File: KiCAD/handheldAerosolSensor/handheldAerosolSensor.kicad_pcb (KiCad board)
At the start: 2 copper layers, 100 x 94.8 mm, 55 parts, among them J1 I2C 3v3, J2 ePaper, J201 PWR-OUT, J202 Ext.Sw, J3 SPS30, J4 BME/P280, J5 Ext.Sw, J6 PMS5003, Q1 AO3401, Q2 BSS138, Q201 AO3401, Q202 BC848, Q203 BC848, Q3 BSS138, SW1 PWR, SW201 PWR, U2 Mini DC-DC Convertor, U202 Mini DC-DC Convertor, U3 ESP32-DEVKIT-V1 30pin

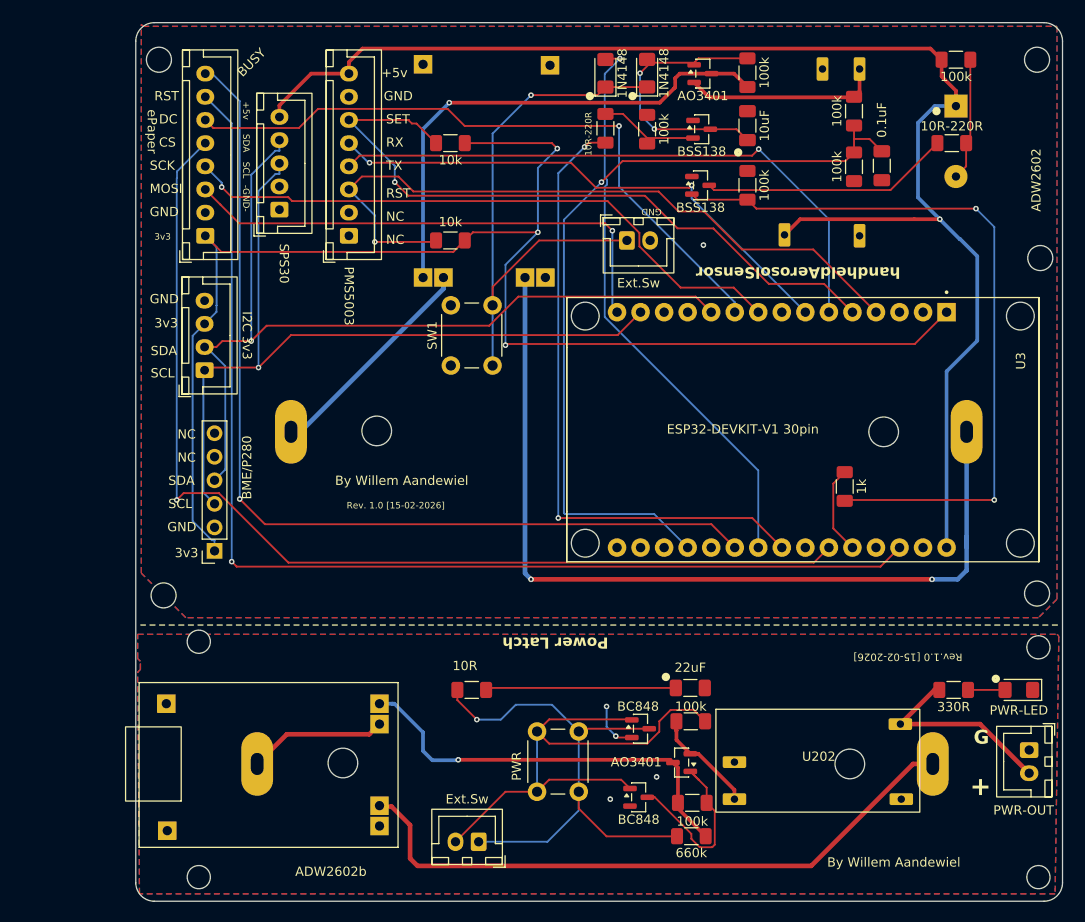
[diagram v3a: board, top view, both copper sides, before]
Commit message: Repositioned all mounting holes (H1-H5, H201-H204) to align with updated mechanical constraints. Updated board edge graphics and coordinates to match the new hole positions. Changes improve PCB fitment in enclosure.
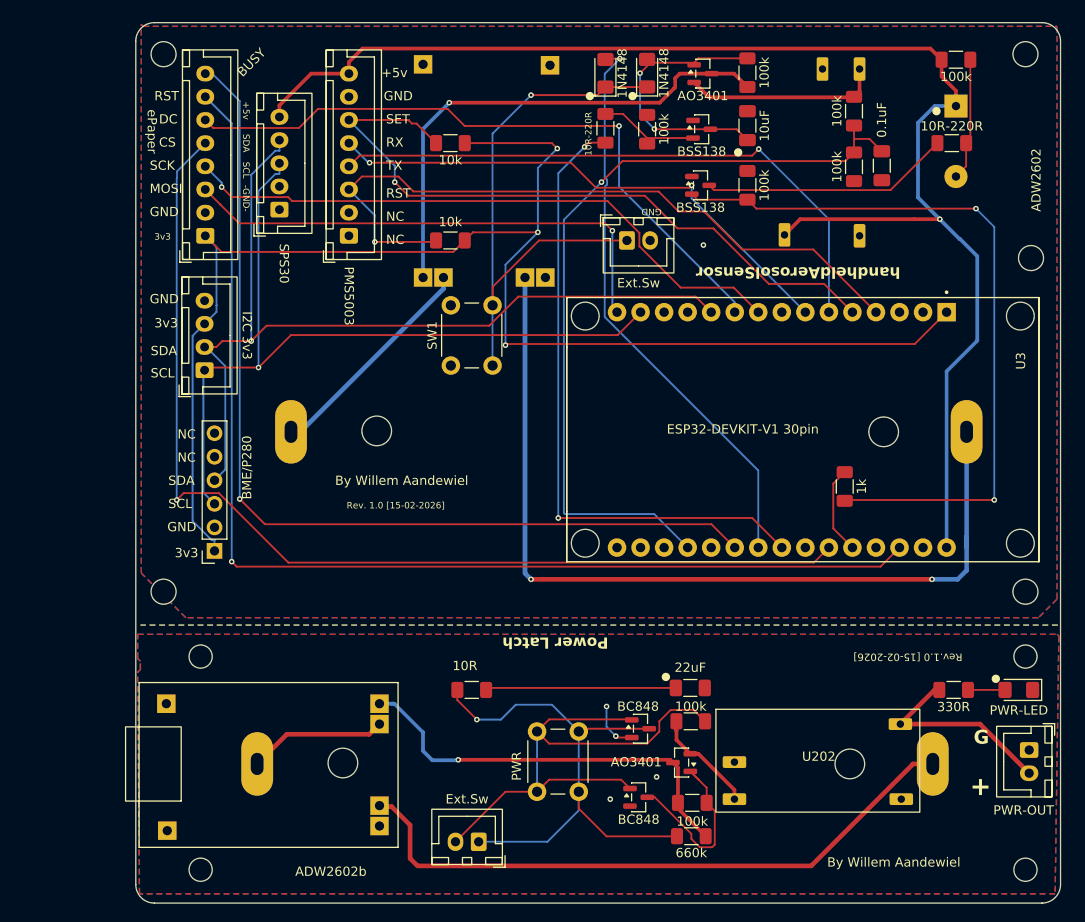
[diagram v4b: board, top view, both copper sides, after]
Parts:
- moved H202 1.72 mm to (223.0, 112.0)
- moved H203 1.61 mm to (223.0, 135.0)
- moved H201 1.61 mm to (134.0, 112.0)
- moved H2 1.39 mm to (223.0, 47.0)
- moved H3 1.27 mm to (223.0, 105.0)
- moved H5 1.00 mm to (223.6, 69.0)
- moved H204 0.82 mm to (134.0, 135.0)
- moved H1 0.78 mm to (130.0, 47.0)
- moved H4 0.40 mm to (130.0, 105.0)
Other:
- board size 100 x 94.8 mm -> 99.8 x 95 mm
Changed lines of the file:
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@@
 	(footprint "MountingHole:MountingHole_2.5mm"
 		(layer "F.Cu")
-		(at 133.8 110.4)
+		(at 134 112)
 		(descr "Mounting Hole 2.5mm, no annular, generated by kicad-footprint-generator mountinghole.py")
 		(tags "mountinghole")
@@
 	(footprint "MountingHole:MountingHole_2.7mm"
 		(layer "F.Cu")
-		(at 224.6 69)
+		(at 223.6 69)
 		(descr "Mounting Hole 2.7mm, no annular, generated by kicad-footprint-generator mountinghole.py")
 		(tags "mountinghole")
@@
 	(footprint "MountingHole:MountingHole_2.5mm"
 		(layer "F.Cu")
-		(at 224.4 111)
+		(at 223 112)
 		(descr "Mounting Hole 2.5mm, no annular, generated by kicad-footprint-generator mountinghole.py")
 		(tags "mountinghole")
@@
 	(footprint "MountingHole:MountingHole_2.5mm"
 		(layer "F.Cu")
-		(at 224.4 135.8)
+		(at 223 135)
 		(descr "Mounting Hole 2.5mm, no annular, generated by kicad-footprint-generator mountinghole.py")
 		(tags "mountinghole")
@@
 	(footprint "MountingHole:MountingHole_2.7mm"
 		(layer "F.Cu")
-		(at 130 105.4)
+		(at 130 105)
 		(descr "Mounting Hole 2.7mm, no annular, generated by kicad-footprint-generator mountinghole.py")
 		(tags "mountinghole")
@@
 	(footprint "MountingHole:MountingHole_2.7mm"
 		(layer "F.Cu")
-		(at 224.25 47.6)
+		(at 223 47)
 		(descr "Mounting Hole 2.7mm, no annular, generated by kicad-footprint-generator mountinghole.py")
 		(tags "mountinghole")
@@
 	(footprint "MountingHole:MountingHole_2.7mm"
 		(layer "F.Cu")
-		(at 224.25 105.2)
+		(at 223 105)
 		(descr "Mounting Hole 2.7mm, no annular, generated by kicad-footprint-generator mountinghole.py")
 		(tags "mountinghole")
@@
 	(footprint "MountingHole:MountingHole_2.5mm"
 		(layer "F.Cu")
-		(at 133.8 135.8)
+		(at 134 135)
 		(descr "Mounting Hole 2.5mm, no annular, generated by kicad-footprint-generator mountinghole.py")
 		(tags "mountinghole")
@@
 	(footprint "MountingHole:MountingHole_2.7mm"
 		(layer "F.Cu")
-		(at 129.5 47.6)
+		(at 130 47)
 		(descr "Mounting Hole 2.7mm, no annular, generated by kicad-footprint-generator mountinghole.py")
 		(tags "mountinghole")
@@
 	)
 	(gr_arc
-		(start 227 136.4)
-		(mid 226.414214 137.814214)
-		(end 225 138.4)
+		(start 127 45.6)
+		(mid 127.585786 44.185786)
+		(end 129 43.6)
 		(stroke
 			(width 0.05)
@@
 		(layer "Edge.Cuts")
 	)
-	(gr_arc
-		(start 129 138.4)
-		(mid 127.585786 137.814214)
-		(end 127 136.4)
+	(gr_line
+		(start 127 136.6)
+		(end 127 45.6)
 		(stroke
 			(width 0.05)
@@
 	)
 	(gr_arc
-		(start 127 45.6)
-		(mid 127.585786 44.185786)
-		(end 129 43.6)
+		(start 226.785786 136.6)
+		(mid 226.2 138.014214)
+		(end 224.785786 138.6)
 		(stroke
 			(width 0.05)
@@
 		(layer "Edge.Cuts")
 	)
-	(gr_line
-		(start 127 136.4)
-		(end 127 45.6)
+	(gr_arc
+		(start 224.785786 43.6)
+		(mid 226.2 44.185786)
+		(end 226.785786 45.6)
 		(stroke
 			(width 0.05)
@@
 	)
 	(gr_line
-		(start 225 138.4)
-		(end 129 138.4)
+		(start 129 43.6)
+		(end 224.785786 43.6)
 		(stroke
 			(width 0.05)
@@
 		(layer "Edge.Cuts")
 	)
-	(gr_line
-		(start 129 43.6)
-		(end 225 43.6)
+	(gr_arc
+		(start 129 138.6)
+		(mid 127.585786 138.014214)
+		(end 127 136.6)
 		(stroke
 			(width 0.05)
@@
 	)
 	(gr_line
-		(start 227 45.6)
-		(end 227 136.4)
+		(start 226.785786 45.6)
+		(end 226.785786 136.6)
 		(stroke
 			(width 0.05)
@@
 		(layer "Edge.Cuts")
 	)
-	(gr_arc
-		(start 225 43.6)
-		(mid 226.414214 44.185786)
-		(end 227 45.6)
+	(gr_line
+		(start 224.785786 138.6)
+		(end 129 138.6)
 		(stroke
 			(width 0.05)
@@
 		(layer "Dwgs.User")
 		(pts
-			(xy 227 45.28) (xy 127.035 45.28)
+			(xy 223.2 108.6) (xy 223.2 123.6)
 		)
-		(height -22.78)
-		(orientation 0)
+		(height 11)
+		(orientation 1)
 		(format
 			(prefix "")
@@
 			(keep_text_aligned yes)
 		)
-		(gr_text "100"
-			(at 177.0175 18.75 0)
+		(gr_text "15"
+			(at 231.8 116.1 90)
 			(layer "Dwgs.User")
 			(effects
 				(font
-					(size 3 3)
-					(thickness 3)
+					(size 2 2)
+					(thickness 0.4)
 					(bold yes)
 				)
@@
 		(layer "Dwgs.User")
 		(pts
-			(xy 223.2 108.6) (xy 223.2 123.6)
+			(xy 223.8 43.6) (xy 223.8 108.6)
 		)
-		(height 11)
+		(height 18.6)
 		(orientation 1)
 		(format
@@
 			(keep_text_aligned yes)
 		)
-		(gr_text "15"
-			(at 231.8 116.1 90)
+		(gr_text "65"
+			(at 238.8 76.1 90)
 			(layer "Dwgs.User")
 			(effects
 				(font
-					(size 2 2)
-					(thickness 0.4)
+					(size 3 3)
+					(thickness 0.6)
 					(bold yes)
 				)
@@
 		(layer "Dwgs.User")
 		(pts
-			(xy 223.8 43.6) (xy 223.8 108.6)
+			(xy 223.2 108.6) (xy 223.2 138.6)
 		)
-		(height 18.6)
+		(height 19.2)
 		(orientation 1)
 		(format
@@
 			(keep_text_aligned yes)
 		)
-		(gr_text "65"
-			(at 238.8 76.1 90)
+		(gr_text "30"
+			(at 238.8 123.6 90)
 			(layer "Dwgs.User")
 			(effects
@@
 		(layer "Dwgs.User")
 		(pts
-			(xy 223.2 108.6) (xy 223.2 138.6)
+			(xy 127 52.4) (xy 226.8 52.4)
 		)
-		(height 19.2)
-		(orientation 1)
+		(height -14.2)
+		(orientation 0)
 		(format
 			(prefix "")
@@
 			(units 3)
 			(units_format 0)
-			(precision 1)
+			(precision 4)
 			(suppress_zeroes yes)
 		)
@@
 			(keep_text_aligned yes)
 		)
-		(gr_text "30"
-			(at 238.8 123.6 90)
+		(gr_text "99.8"
+			(at 176.9 37.05 0)
 			(layer "Dwgs.User")
 			(effects
 				(font
-					(size 3 3)
-					(thickness 0.6)
-					(bold yes)
+					(size 1 1)
+					(thickness 0.15)
 				)
 			)

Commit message: KiCAD design openScad design
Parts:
- removed BT201: BH-18650-PC, MyNewLibrary:BAT_BH-18650-PC
- removed C201: 22uF, Capacitor_SMD:C_1206_3216Metric_Pad1.33x1.80mm_HandSolder
- removed D201: PWR-LED, LED_SMD:LED_1206_3216Metric_Pad1.42x1.75mm_HandSolder
- removed H201, H202, H203, H204: MountingHole, MountingHole:MountingHole_2.5mm
- removed J201: PWR-OUT, Connector_JST:JST_XH_B2B-XH-A_1x02_P2.50mm_Vertical
- removed J202: Ext.Sw, Connector_JST:JST_XH_B2B-XH-A_1x02_P2.50mm_Vertical
- removed Q1, Q201: AO3401, Package_TO_SOT_SMD:SOT-23
- removed Q2, Q3: BSS138, Package_TO_SOT_SMD:SOT-23
- removed Q202, Q203: BC848, Package_TO_SOT_SMD:SOT-23
- removed R201, R202: 100k, Resistor_SMD:R_1206_3216Metric_Pad1.30x1.75mm_HandSolder
- removed R203: 660k, Resistor_SMD:R_1206_3216Metric_Pad1.30x1.75mm_HandSolder
- removed R204: 330R, Resistor_SMD:R_1206_3216Metric_Pad1.30x1.75mm_HandSolder
- removed R205: 10R, Resistor_SMD:R_1206_3216Metric_Pad1.30x1.75mm_HandSolder
- removed SW201: PWR, Button_Switch_THT:SW_PUSH_6mm_H4.3mm
- removed U201: ~, MyNewLibrary:TP4056_USB-Charger_Board
- removed U202: Mini DC-DC Convertor, MyNewLibrary:Mini DC-DC Boost Convertor
- added Q101: AO3401A, MyNewLibrary:AO3401, F.Cu at (188.8, 49.2)
- added Q102: BSS138, MyNewLibrary:BSS138, F.Cu at (188.8, 61.2)
- added Q103: BSS138, MyNewLibrary:BSS138, F.Cu at (188.8, 55.0)
- moved J4 22.4 mm to (157.8, 102.5), turned to -90 degrees
- moved J1 9.82 mm to (133.8, 90.9)
- moved J2 9.82 mm to (133.9, 76.4)
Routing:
- net B2BAT-: track 69.1 -> 0.00 mm
- net Net-(J202-Pin_2): track 61.5 -> 0.00 mm
- net Net-(J202-Pin_1): track 59.0 -> 0.00 mm, vias 1 -> 0
- net OUT2+: track 45.0 -> 0.00 mm, vias 1 -> 0
- net SDA: track 96.7 -> 119.0 mm, vias 1 -> 0
- net +B5v: track 21.8 -> 0.00 mm
- net Net-(C201-Pad1): track 20.6 -> 0.00 mm
- net Net-(Q201-G): track 20.2 -> 0.00 mm
- net SCL: track 87.8 -> 103.9 mm, vias 1 -> 2
- net B2BAT+: track 15.0 -> 0.00 mm
- net PWR: track 12.5 -> 0.00 mm
- net EPD_CS: track 114.2 -> 102.6 mm
- net 3v3: track 157.0 -> 146.8 mm, vias 3 -> 4
- net EPD_RST: track 124.5 -> 117.1 mm
- net EPD_MOSI(DIN): track 54.8 -> 48.3 mm, vias 1 -> 0
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- removed copper zone on B.Cu, net GND2
- removed copper zone on F.Cu, net GND2
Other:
- board size 99.8 x 95 mm -> 99.8 x 65 mm
- board text added: "Rev. 2.0 [11-03-2026]"
- board text removed: "ADW2602b"
- board text removed: "G"
- board text removed: "Power Latch"
- board text removed: "Rev. 1.0 [15-02-2026]"
- board text removed: "Rev.1.0 [15-02-2026]"
